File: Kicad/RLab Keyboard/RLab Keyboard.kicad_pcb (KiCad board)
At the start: 2 copper layers, 100 x 100 mm, 75 parts, among them J1 Conn_01x01_Pin, J10 Conn_01x01_Pin, J11 Conn_01x01_Pin, J12 Conn_01x01_Pin, J13 Conn_01x04, J14 Conn_01x07, J15 Conn_01x03, J16 AudioJack3_Switch, J17 Conn_01x03, J18 Conn_01x03, J19 Conn_01x09, J2 Conn_01x01_Pin, J3 Conn_01x01_Pin, J4 Conn_01x01_Pin, J5 Conn_01x01_Pin, J6 Conn_01x01_Pin, J7 Conn_01x01_Pin, J8 Conn_01x01_Pin, J9 Conn_01x01_Pin, SW1 SW_MEC_5G, SW2 SW_MEC_5G, U1 MPR121QR2, U2 LP5907MFX-3.3, U3 74LVC1G17, U4 PCM5102, U5 LM386

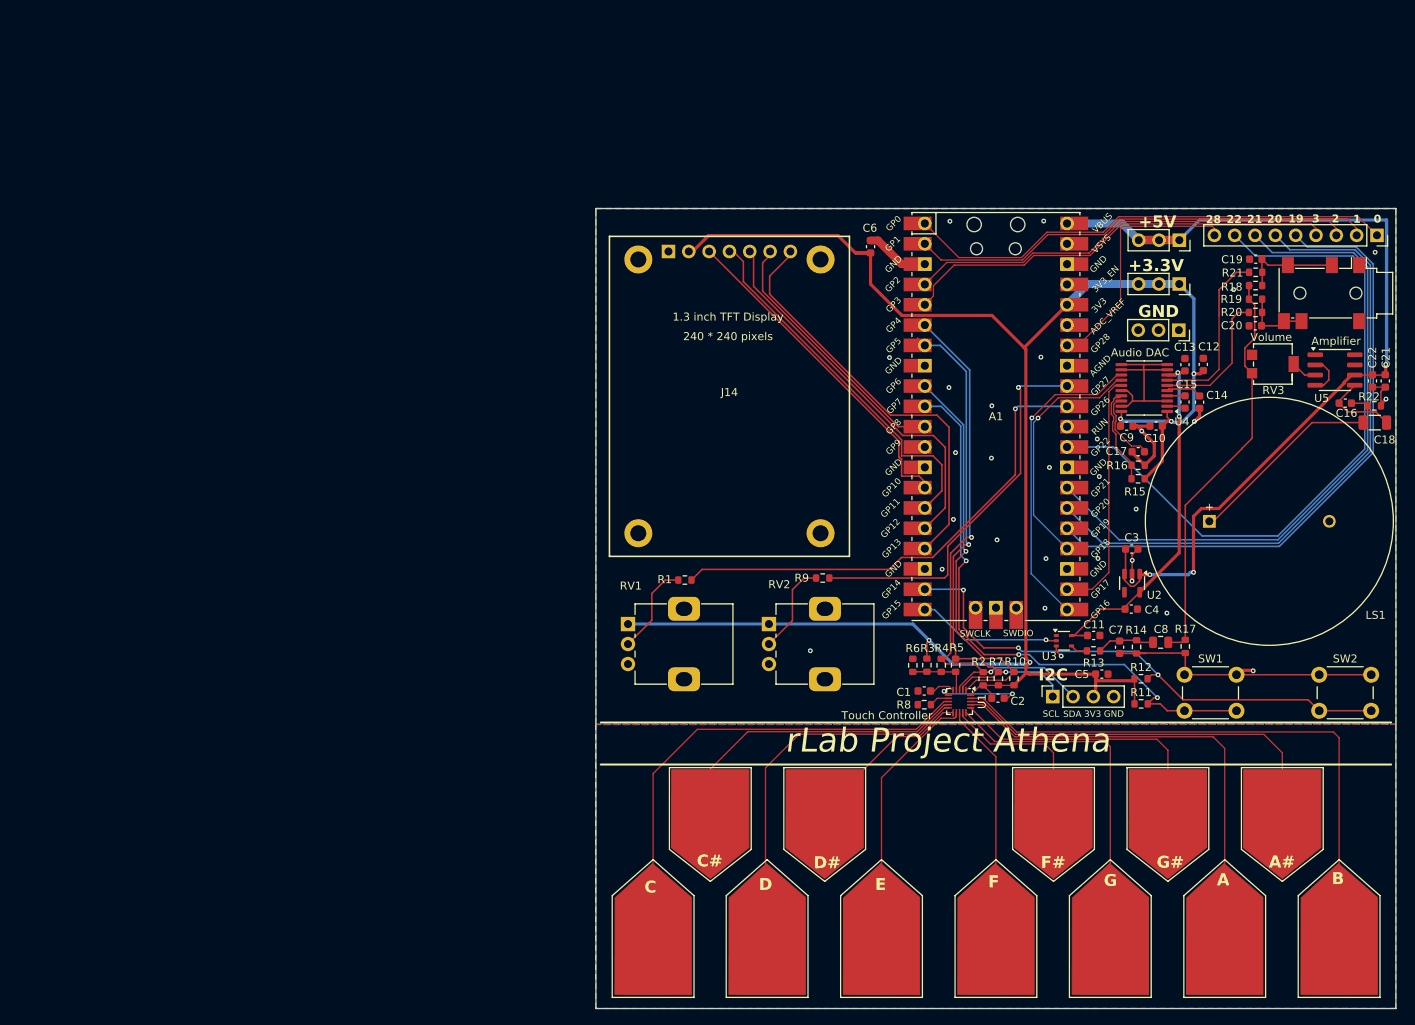
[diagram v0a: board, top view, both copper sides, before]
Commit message: Initial submit of version 1.2
Update to layout of Kicad files for new user interface
Added circuit Python test firmware
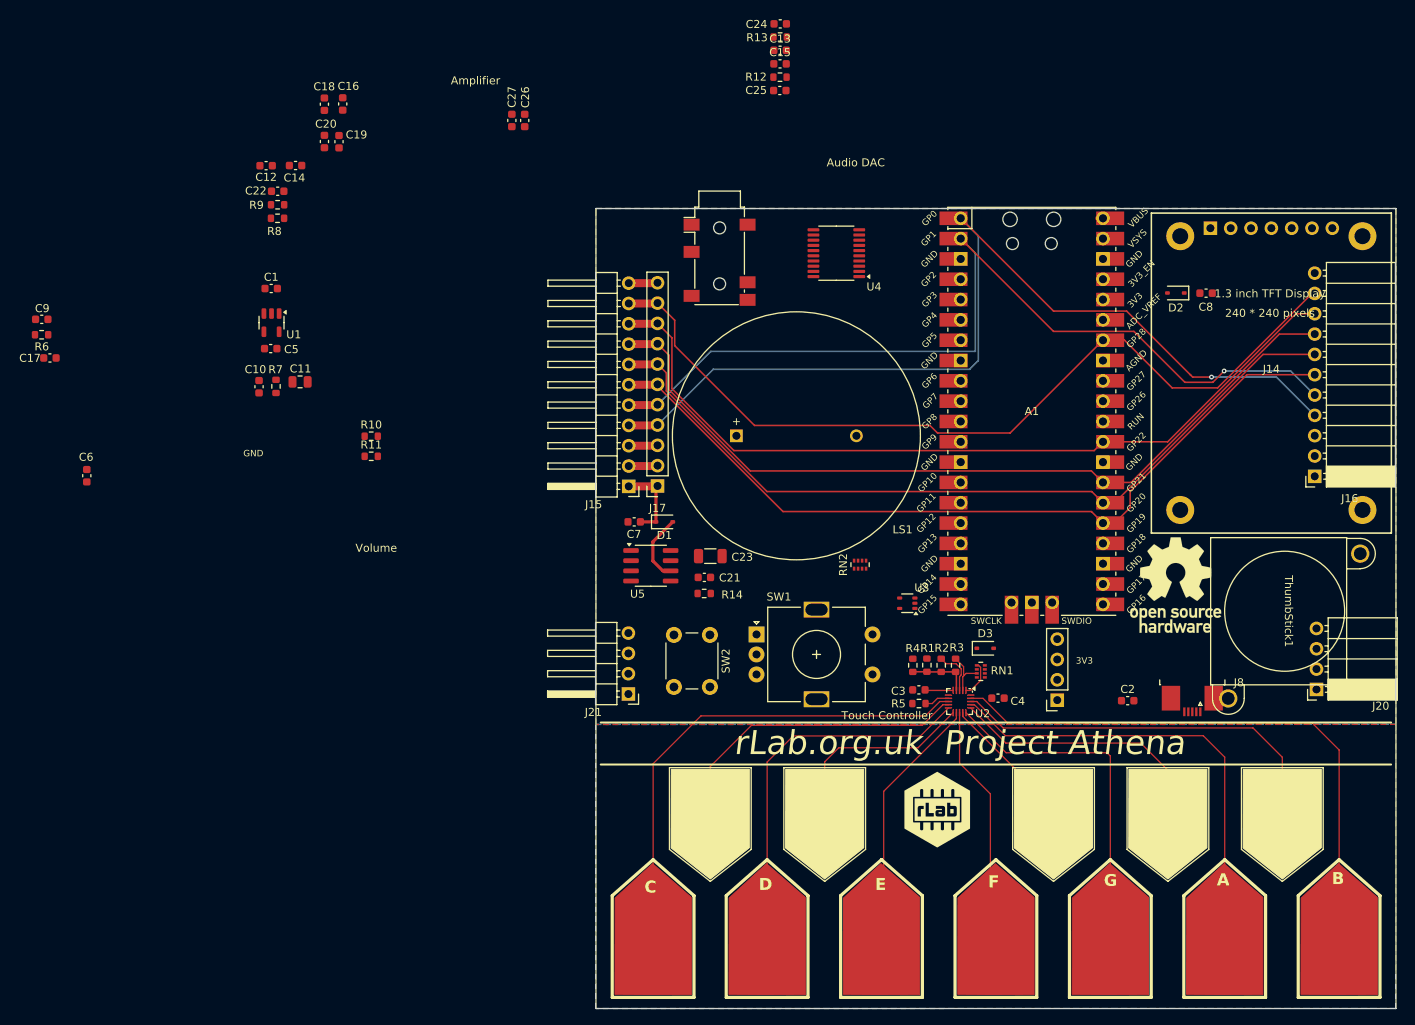
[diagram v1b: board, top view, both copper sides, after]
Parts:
- removed the J18 at (172.9, 65.2)
- removed the J19 at (197.6, 53.4)
- removed the R1 at (111.1, 96.4)
- removed the R12 at (168.1, 108.8)
- removed R17: 1k8, Resistor_SMD:R_0603_1608Metric
- removed the R2 at (148.4, 108.8)
- removed the R7 at (150.3, 108.8)
- removed the R9 at (128.3, 96.2)
- removed RV1, RV2: 10k, rLab_Keyboard:Potentiometer_Alps_RK09K_Single_Vertical
- removed RV3: 10k, rLab_Keyboard:Potentiometer_Bourns_3214G_Horizontal
- removed the SW2 at (190.4, 108.3)
- added C2: 1u, Capacitor_SMD:C_0603_1608Metric, F.Cu at (166.5, 111.5)
- added C7: 2u2, Capacitor_SMD:C_0603_1608Metric, F.Cu at (104.8, 89.2)
- added C8: 2u2, Capacitor_SMD:C_0603_1608Metric, F.Cu at (176.3, 60.6)
- added D1: D, Diode_SMD:D_SOD-323, F.Cu at (108.6, 89.2)
- added D2: D, Diode_SMD:D_SOD-323, F.Cu at (172.5, 60.6)
- added D3: D, Diode_SMD:D_SOD-323, F.Cu at (148.7, 105.0)
- added J16: Conn_01x13, Connector_PinSocket_2.54mm:PinSocket_1x11_P2.54mm_Horizontal, F.Cu at (189.8, 83.5)
- added J20: Conn_01x04, Connector_PinSocket_2.54mm:PinSocket_1x04_P2.54mm_Horizontal, F.Cu at (190.1, 110.1)
- added J21: Conn_01x04, Connector_PinHeader_2.54mm:PinHeader_1x04_P2.54mm_Horizontal, F.Cu at (104.1, 110.7)
- added J8: Conn_01x05, Connector_FFC-FPC:TE_0-1734839-5_1x05-1MP_P0.5mm_Horizontal, F.Cu at (174.6, 111.6)
- added RN1: R_Network04, Resistor_SMD:R_Array_Concave_4x0402, F.Cu at (148.1, 107.9)
- added RN2: R_Network04, Resistor_SMD:R_Array_Concave_4x0402, F.Cu at (133.0, 94.5)
- added SW1: RotaryEncoder_Switch_MP, rLab_Keyboard:RotaryEncoder_Alps_EC11E-Switch_Vertical_H20mm, F.Cu at (120.1, 103.2)
- added SYM1: Logo_Open_Hardware_Small, Symbol:OSHW-Logo_11.4x12mm_SilkScreen, F.Cu at (172.5, 97.1)
- added ThumbStick1: ~, rLab_Keyboard:Thumb_stick, F.Cu at (186.1, 100.3)
- A1: footprint Pi_Pico2:RPi_Pico_SMD_TH -> rLab_Keyboard:RPi_Pico_SMD_TH
- C13: renamed from R18; value 0R -> 100n; footprint Resistor_SMD:R_0603_1608Metric -> Capacitor_SMD:C_0603_1608Metric
- C15: renamed from R19; value 0R -> 100n; footprint Resistor_SMD:R_0603_1608Metric -> Capacitor_SMD:C_0603_1608Metric
- J10: renamed from J9; footprint rLab_Keyboard:Black_key -> rLab_Keyboard:Black_key_fill
- J11: renamed from J10; footprint rLab_Keyboard:Black_key -> rLab_Keyboard:Black_key_fill
- J12: renamed from J11; footprint rLab_Keyboard:Black_key -> rLab_Keyboard:Black_key_fill
- J13: renamed from J12; footprint rLab_Keyboard:Black_key -> rLab_Keyboard:Black_key_fill
- J15: value Conn_01x03 -> Conn_01x13; footprint Connector_PinSocket_2.54mm:PinSocket_1x03_P2.54mm_Vertical -> Connector_PinHeader_2.54mm:PinHeader_1x11_P2.54mm_Horizontal
- J17: value Conn_01x03 -> Conn_01x13; footprint Connector_PinSocket_2.54mm:PinSocket_1x03_P2.54mm_Vertical -> Connector_PinSocket_2.54mm:PinSocket_1x11_P2.54mm_Vertical
- J9: renamed from J8; footprint rLab_Keyboard:Black_key -> rLab_Keyboard:Black_key_fill
- R10, R11: value 4k7 -> 1k
- R12: renamed from R20; value 470 -> 470R
- R13: renamed from R21; value 470 -> 470R
- R14: renamed from R22; value 10 -> 10R
- R6: renamed from R13; value 220 -> 220R
- R7: renamed from R14; value 100 -> 100R
- R8: renamed from R15; value 100 -> 100R
- R9: renamed from R16; value 100 -> 100R
- moved C17 137.3 mm to (31.8, 68.7)
- moved C9 137.3 mm to (30.7, 63.9)
- moved R6 137.3 mm to (30.7, 65.8)
- moved R7 112.4 mm to (60.0, 72.2)
- moved C10 112.4 mm to (57.9, 72.3)
- moved C14 112.4 mm to (62.5, 44.6)
- moved C19 112.4 mm to (67.9, 41.6)
- moved C27 112.4 mm to (89.5, 39.0)
- moved R8 112.4 mm to (60.2, 51.2)
- moved U1 112.4 mm to (59.5, 64.3)
- moved C1 112.4 mm to (59.4, 60.0)
- moved C11 112.4 mm to (63.0, 71.7)
- moved C12 112.4 mm to (58.8, 44.6)
- moved C16 112.4 mm to (68.3, 36.9)
- moved C18 112.4 mm to (66.1, 37.0)
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- renumbered C3 to C1, C7 to C10, C8 to C11, C9 to C12, C10 to C14, C12 to C16, C5 to C17, C13 to C18, C14 to C19, C15 to C20, C16 to C21, C17 to C22, C18 to C23, C19 to C24, C20 to C25, C21 to C26, C22 to C27, C1 to C3, C2 to C4, C4 to C5, C11 to C9, J16 to J18, J13 to J19, R3 to R1, R4 to R2, R5 to R3, R6 to R4, R8 to R5, SW1 to SW2, U2 to U1, U1 to U2
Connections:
- A1 pad 12: unconnected-(A1-GPIO9-Pad12)_1 -> /Joy_Sw
- A1 pad 19: /Button2 -> /Enc_Sw
- A1 pad 31: /Pot1 -> /U/D
- A1 pad 32: /Pot2 -> /L/R
- A1 pad 4: /GPIO2 -> /Enc_A
- A1 pad 5: /GPIO3 -> /Enc_B
- C11 pad 1: Net-(C8-Pad1) -> Net-(C11-Pad1)
- C13 pad 1: Net-(C8-Pad1) -> Net-(C11-Pad1)
- C13 pad 2: /ROUT -> Net-(C13-Pad2)
- C15 pad 1: Net-(C8-Pad1) -> Net-(C11-Pad1)
- C15 pad 2: /LOUT -> Net-(C15-Pad2)
- C17 pad 2: +3.3V -> Net-(D3-K)
- J15 pad 1: +3.3V -> Net-(D1-K)
- J15 pad 2: +3.3V -> Net-(D2-K)
- J15 pad 3: +3.3V -> GND
- J17 pad 1: +5V -> Net-(D1-K)
- J17 pad 2: +5V -> Net-(D2-K)
- J17 pad 3: +5V -> GND
- J18 pad 6: /ROUT -> Net-(C13-Pad2)
- J18 pad 7: /LOUT -> Net-(C15-Pad2)
- J19 pad 3: +3.3V -> Net-(D3-K)
- R10 pad 1: +3.3V -> Net-(U5-+)
- R10 pad 2: /IRQ -> Net-(C11-Pad1)
- R11 pad 1: +3.3V -> Net-(U5-+)
- R11 pad 2: /Button1 -> GND
- SW2 pad 1: GND -> /Button1
- SW2 pad 2: /Button1 -> GND
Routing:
- net +3.3V: track 241.6 -> 0.00 mm, vias 5 -> 0
- net +5V: track 118.5 -> 9.10 mm, vias 3 -> 0
- net GND: track 112.4 -> 7.24 mm, vias 31 -> 0
- net /GPIO28: track 30.2 -> 106.5 mm
- net /Button1: track 72.9 -> 0.00 mm, vias 3 -> 0
- net /Button2: track 66.4 -> 0.00 mm, vias 3 -> 0
- net /SDA: track 70.3 -> 5.81 mm, vias 2 -> 0
- net /SCL: track 68.1 -> 6.20 mm, vias 2 -> 0
- net /Pot1: track 60.8 -> 0.00 mm, vias 1 -> 0
- net /GPIO0: track 61.4 -> 120.3 mm, vias 0 -> 1
- net /GPIO1: track 57.4 -> 114.5 mm, vias 0 -> 1
- net /GPIO2: track 55.1 -> 0.00 mm
- net /BL: track 54.8 -> 0.00 mm
- net /GPIO3: track 54.1 -> 0.00 mm
- net Net-(C8-Pad1): track 51.6 -> 0.00 mm
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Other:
- board text added: "rLab.org.uk Project Athena"
- board text removed: "+3.3V"
- board text removed: "+5V"
- board text removed: "0"
- board text removed: "1"
- board text removed: "19"
- board text removed: "2"
- board text removed: "20"
- board text removed: "21"
- board text removed: "22"
- board text removed: "28"
- board text removed: "3"
- board text removed: "I2C"
- board text removed: "SCL"
- board text removed: "SDA"
- board text removed: "rLab Project Athena"

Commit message: Latest rLab Keyboard layout
Added connectors for joining boards
Swap display and speaker.
New control layout
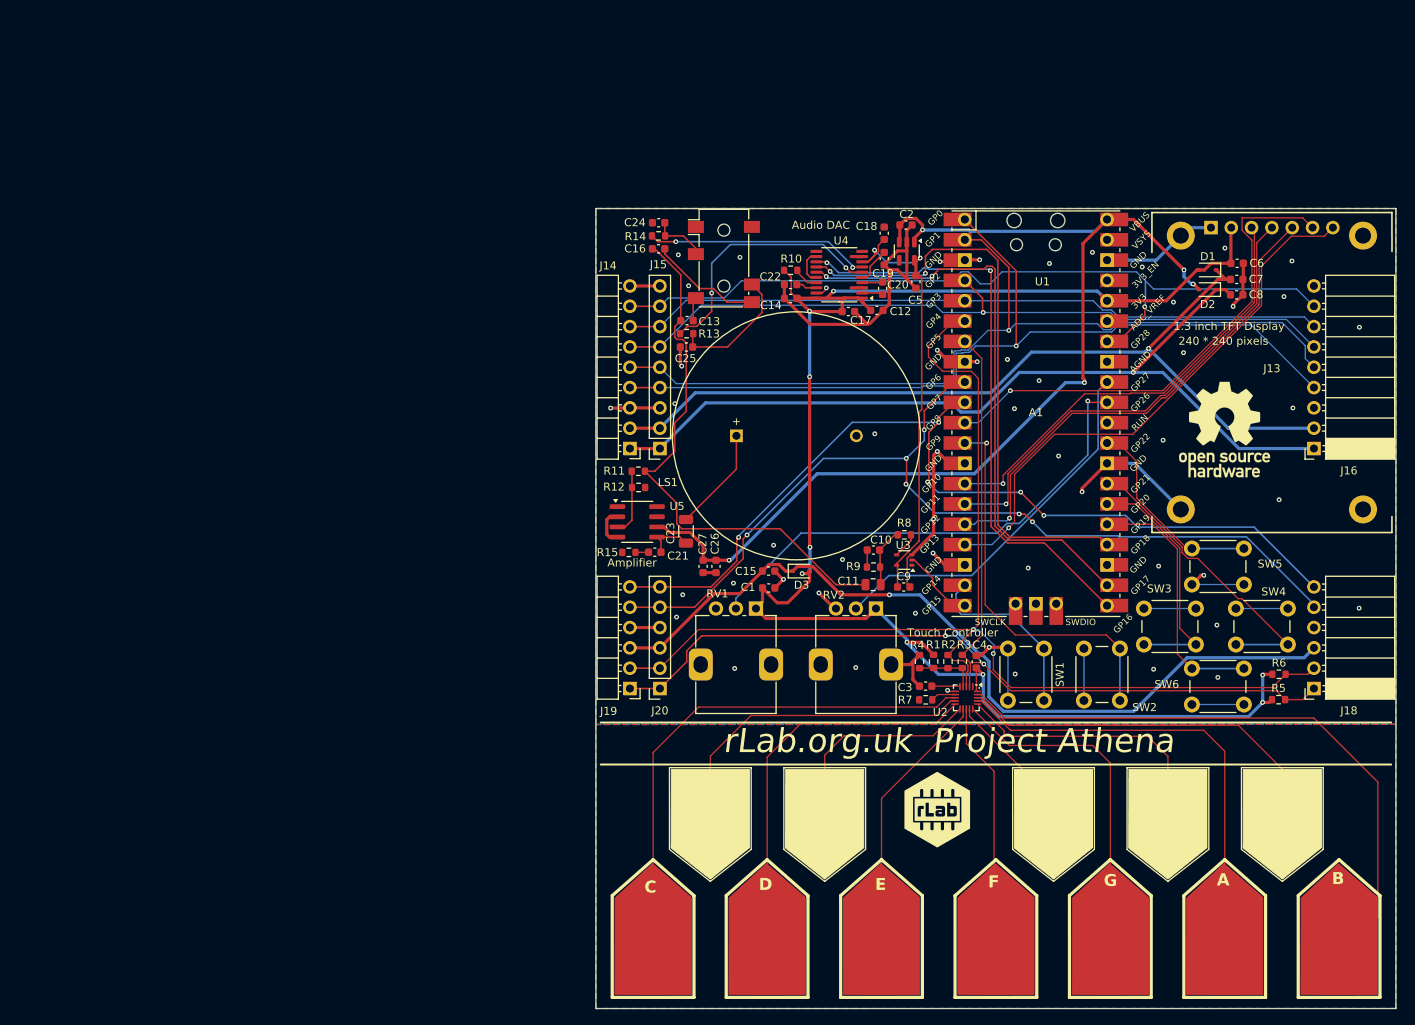
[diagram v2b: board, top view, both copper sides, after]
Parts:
- removed the J17 at (107.7, 84.7)
- removed J21: Conn_01x04, Connector_PinHeader_2.54mm:PinHeader_1x04_P2.54mm_Horizontal
- removed the J8 at (174.6, 111.6)
- removed the R9 at (60.2, 49.5)
- removed RN1, RN2: R_Network04, Resistor_SMD:R_Array_Concave_4x0402
- removed the SW1 at (120.1, 103.2)
- removed ThumbStick1: ~, rLab_Keyboard:Thumb_stick
- added J14: Conn_01x09, rLab_Keyboard:PinHeader_1x09_P2.54mm_Horizontal, F.Cu at (104.2, 80.0)
- added J18: Conn_01x06, Connector_PinSocket_2.54mm:PinSocket_1x06_P2.54mm_Horizontal, F.Cu at (189.8, 110.0)
- added R5: 4k7, Resistor_SMD:R_0603_1608Metric, F.Cu at (185.3, 111.4)
- added R6: 4k7, Resistor_SMD:R_0603_1608Metric, F.Cu at (185.4, 108.2)
- added RV1: 10k, rLab_Keyboard:Potentiometer_Alps_RK09K_Single_Vertical, F.Cu at (120.0, 100.0)
- added RV2: 10k, rLab_Keyboard:Potentiometer_Alps_RK09K_Single_Vertical, F.Cu at (135.0, 100.0)
- added SW2: SW_MEC_5G, Button_Switch_THT:SW_PUSH_6mm_H8mm, F.Cu at (165.5, 105.0)
- added SW3: SW_MEC_5G, Button_Switch_THT:SW_PUSH_6mm_H8mm, F.Cu at (175.0, 104.5)
- added SW4: SW_MEC_5G, Button_Switch_THT:SW_PUSH_6mm_H8mm, F.Cu at (186.5, 104.5)
- added SW5: SW_MEC_5G, Button_Switch_THT:SW_PUSH_6mm_H8mm, F.Cu at (174.5, 92.5)
- added SW6: SW_MEC_5G, Button_Switch_THT:SW_PUSH_6mm_H8mm, F.Cu at (174.5, 107.5)
- J15: value Conn_01x13 -> Conn_01x09; footprint Connector_PinHeader_2.54mm:PinHeader_1x11_P2.54mm_Horizontal -> Connector_PinSocket_2.54mm:PinSocket_1x09_P2.54mm_Vertical
- J16: value Conn_01x13 -> Conn_01x09; footprint Connector_PinSocket_2.54mm:PinSocket_1x11_P2.54mm_Horizontal -> Connector_PinSocket_2.54mm:PinSocket_1x09_P2.54mm_Horizontal
- J19: value Conn_01x04 -> Conn_01x06; footprint Connector_PinSocket_2.54mm:PinSocket_1x04_P2.54mm_Vertical -> rLab_Keyboard:PinHeader_1x06_P2.54mm_Horizontal
- J20: value Conn_01x04 -> Conn_01x06; footprint Connector_PinSocket_2.54mm:PinSocket_1x04_P2.54mm_Horizontal -> Connector_PinSocket_2.54mm:PinSocket_1x06_P2.54mm_Vertical
- SW1: renamed from SW2; footprint Button_Switch_THT:SW_PUSH_6mm_H5mm -> Button_Switch_THT:SW_PUSH_6mm_H8mm
- moved C6 146.2 mm to (180.2, 56.9), turned to 180 degrees
- moved C9 112.8 mm to (138.5, 97.3)
- moved R8 110.7 mm to (138.6, 90.8), turned to 0 degrees
- moved C15 93.7 mm to (121.6, 95.3)
- moved J20 82.1 mm to (108.0, 110.0)
- moved C7 81.2 mm to (180.1, 58.9), turned to 180 degrees
- moved C5 81.1 mm to (140.0, 59.2), turned to -90 degrees
- moved U1 79.9 mm to (138.9, 55.3)
- moved C2 79.7 mm to (138.8, 52.1)
- moved C10 79.5 mm to (134.7, 92.7), turned to 0 degrees
- moved C12 78.5 mm to (135.1, 62.7)
- moved R9 78.0 mm to (134.7, 94.8), turned to 180 degrees
- moved C11 76.0 mm to (134.7, 97.0), turned to 0 degrees
- moved D1 74.9 mm to (176.5, 57.7), turned to 180 degrees
- moved C20 72.1 mm to (135.8, 60.0)
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- renumbered C2 to C1, C17 to C15, C15 to C16, C16 to C17, C1 to C2, J11 to J10, J12 to J11, J13 to J12, J14 to J13, J18 to J17, J9 to J8, J10 to J9, R8 to R10, R10 to R11, R11 to R12, R12 to R13, R13 to R14, R14 to R15, R5 to R7, R6 to R8, R7 to R9
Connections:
- A1 pad 10: /Button1 -> /SW4
- A1 pad 12: /Joy_Sw -> /SW2
- A1 pad 19: /Enc_Sw -> /SW1
- A1 pad 25: /GPIO19 -> /DPAD_D
- A1 pad 26: /GPIO20 -> /DPAD_L
- A1 pad 27: /GPIO21 -> /DPAD_R
- A1 pad 29: /GPIO22 -> /DPAD_U
- A1 pad 31: /U/D -> /POTA_1
- A1 pad 32: /L/R -> /POTA_2
- A1 pad 4: /Enc_A -> /GPIO2
- A1 pad 5: /Enc_B -> /GPIO3
- A1 pad 9: /IRQ -> /SW3
- D1 pad 2: +5V -> +3.3V
- D2 pad 2: +3.3V -> +5V
- J15 pad 1: Net-(D1-K) -> Net-(D2-K)
- J15 pad 2: Net-(D2-K) -> Net-(D1-K)
- J15 pad 6: /GPIO19 -> /GPIO2
- J15 pad 7: /GPIO20 -> /GPIO3
- J15 pad 8: /GPIO21 -> /GPIO28
- J15 pad 9: /GPIO22 -> GND
- J16 pad 1: Net-(D1-K) -> Net-(D2-K)
- J16 pad 2: Net-(D2-K) -> Net-(D1-K)
- J16 pad 6: /GPIO19 -> /GPIO2
- J16 pad 7: /GPIO20 -> /GPIO3
- J16 pad 8: /GPIO21 -> /GPIO28
- J16 pad 9: /GPIO22 -> GND
- SW1 pad 1: /Button1 -> /SW1
- U2 pad 1: /IRQ -> unconnected-(U2-~{IRQ}-Pad1)
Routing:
- net +3.3V: track 0.00 -> 214.7 mm, vias 0 -> 9
- net GND: track 7.24 -> 209.9 mm, vias 0 -> 53
- net /SDA: track 5.81 -> 149.9 mm, vias 0 -> 2
- net /SCL: track 6.20 -> 140.2 mm, vias 0 -> 2
- net +5V: track 9.10 -> 134.8 mm, vias 0 -> 5
- net /SW3: track 0.00 -> 118.0 mm, vias 0 -> 6
- net /SW4: track 0.00 -> 115.3 mm, vias 0 -> 5
- net Net-(D2-K): track 3.62 -> 111.0 mm, vias 0 -> 1
- net Net-(D3-K): track 0.00 -> 103.8 mm, vias 0 -> 1
- net /GPIO22: track 103.2 -> 0.00 mm
- net /GPIO21: track 103.2 -> 0.00 mm
- net /GPIO20: track 102.0 -> 0.00 mm
- net /GPIO19: track 101.9 -> 0.00 mm
- net Net-(D1-K): track 10.1 -> 110.1 mm, vias 0 -> 1
- net /GPIO2: track 0.00 -> 94.9 mm, vias 0 -> 1
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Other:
- board text removed: "3V3"
- board text removed: "A#"
- board text removed: "C#"
- board text removed: "D#"
- board text removed: "F#"
- board text removed: "G#"
- board text removed: "GND"
- board text removed: "Volume"
